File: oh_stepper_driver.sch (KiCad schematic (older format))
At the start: 27 parts, among them P1 CONN_01X04, Q1 CSD18531Q5A, Q2 CSD18531Q5A, Q3 CSD18531Q5A, Q4 CSD18531Q5A, Q5 CSD18531Q5A, Q6 CSD18531Q5A, Q7 CSD18531Q5A, Q8 CSD18531Q5A, U1 DRV8711

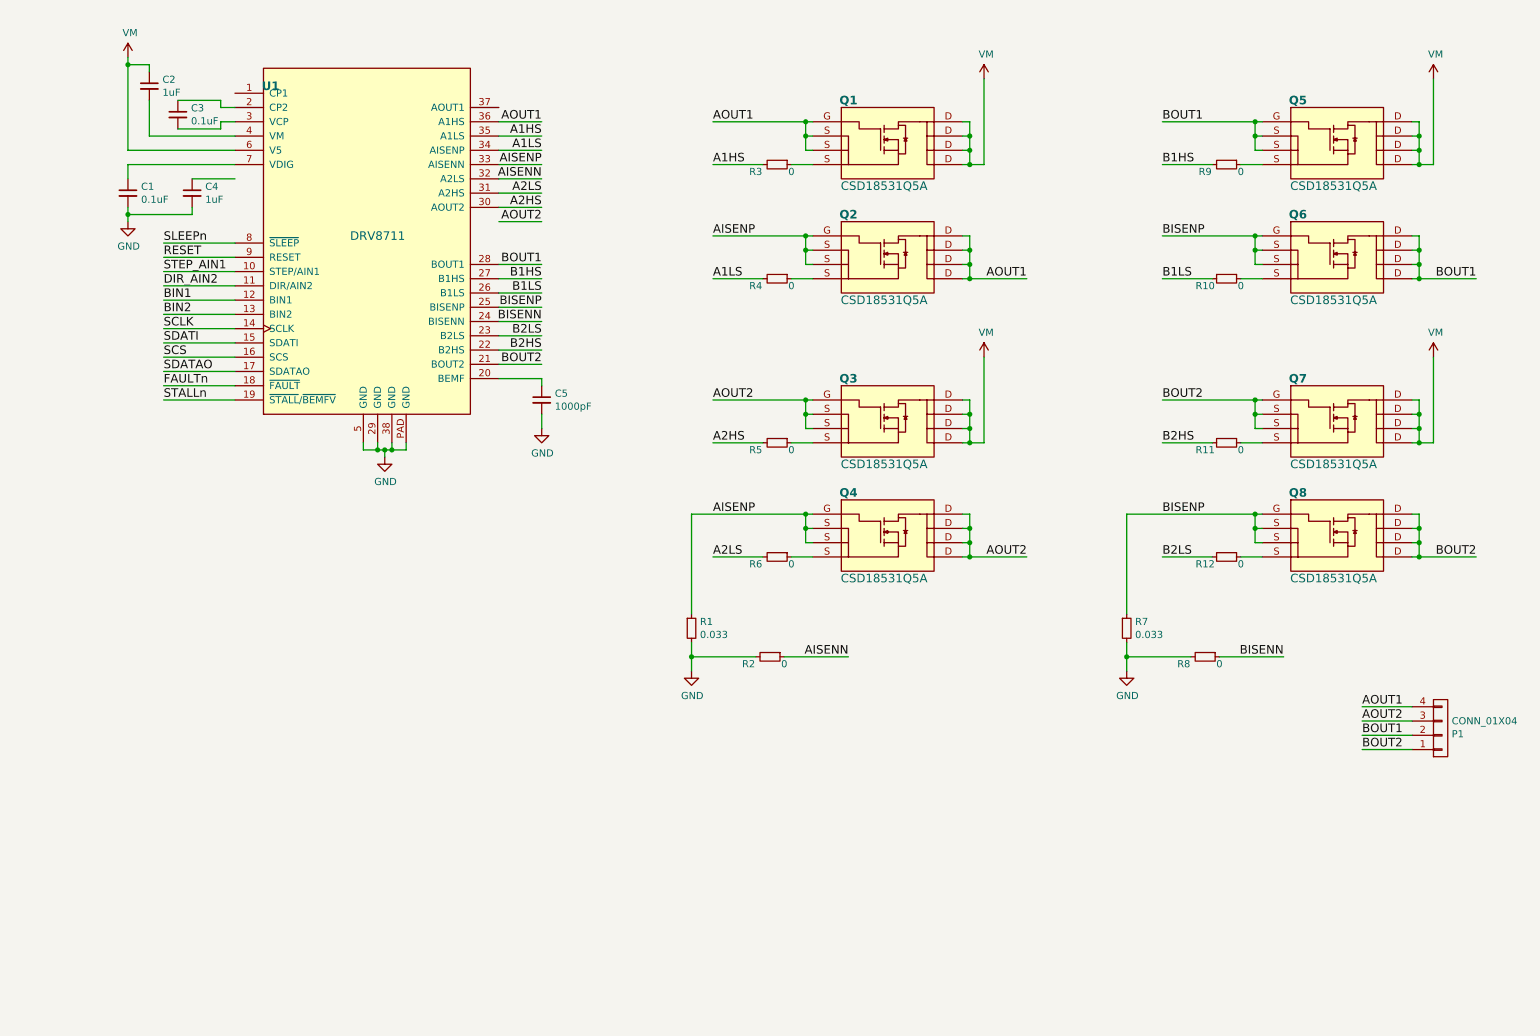
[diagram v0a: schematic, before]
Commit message: FETs sheet added
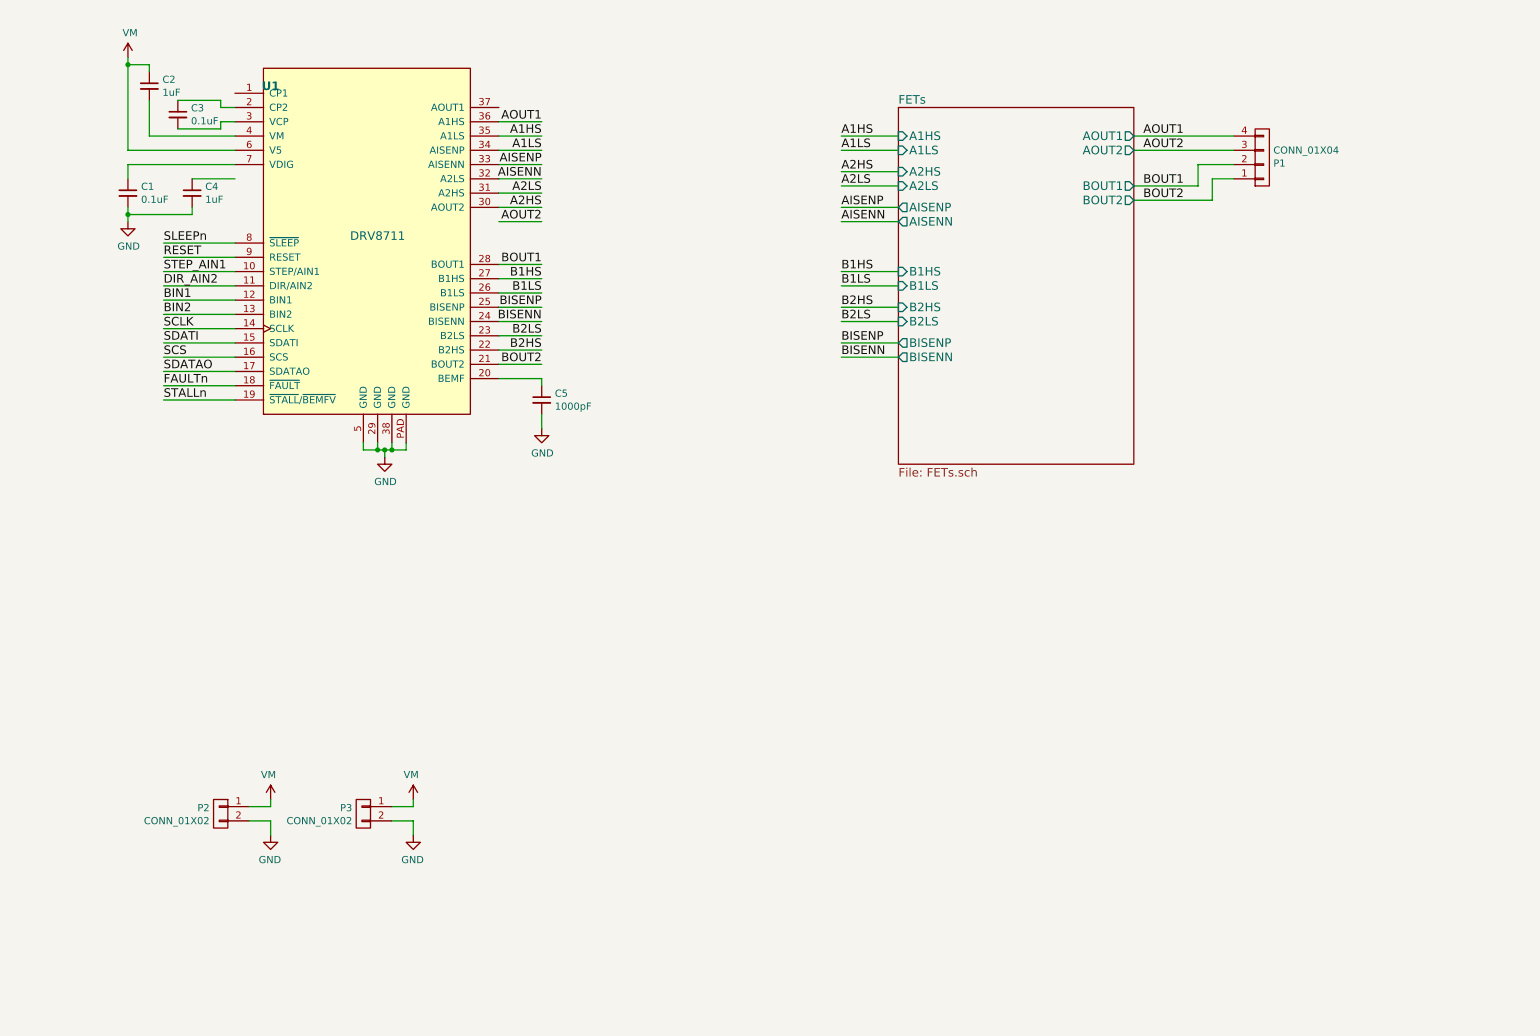
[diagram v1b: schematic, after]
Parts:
- removed Q1, Q2, Q3, Q4, Q5, Q6, Q7, Q8: CSD18531Q5A, oh_stepper:SON5x6_FET, symbol CSD18531Q5A
- removed R1, R7: 0.033, Resistors_SMD:R_2816, symbol R_Small
- removed R10, R11, R12, R3, R4, R5, R6, R9: 0, Resistors_SMD:R_0402, symbol R_Small
- removed R2, R8: 0, Resistors_SMD:R_0603, symbol R_Small
- added P2, P3: CONN_01X02, Connectors:bornier2, symbol CONN_01X02
- C5: footprint (none) -> Capacitors_SMD:C_0402
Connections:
- net GND: now also P2.2 (P2), P3.2 (P2)
- net VM: now also P2.1 (P1), P3.1 (P1)

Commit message: adding decoupling filters
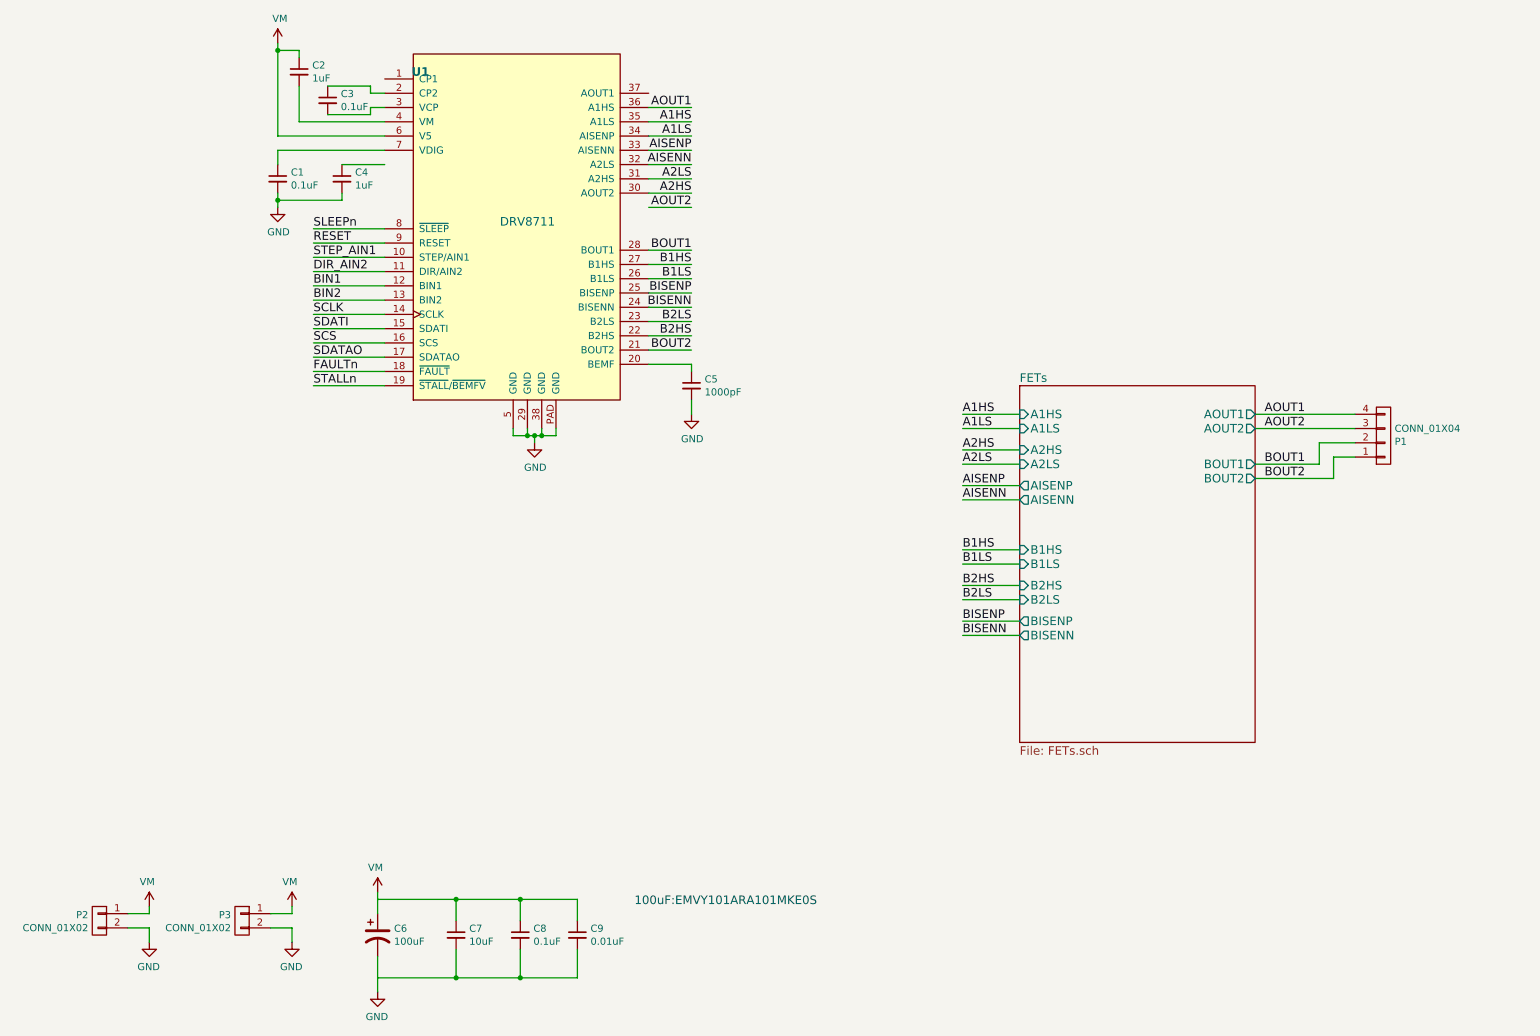
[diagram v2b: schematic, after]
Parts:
- added C6: 100uF, symbol CP1
- added C7: 10uF, symbol C_Small
- added C8: 0.1uF, symbol C_Small
- added C9: 0.01uF, symbol C_Small
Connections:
- wire segments 83 -> 93
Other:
- note added: "100uF:EMVY101ARA101MKE0S"
- moved on the sheet: C1, C2, C3, C4, C5, P1, P2, P3, U1

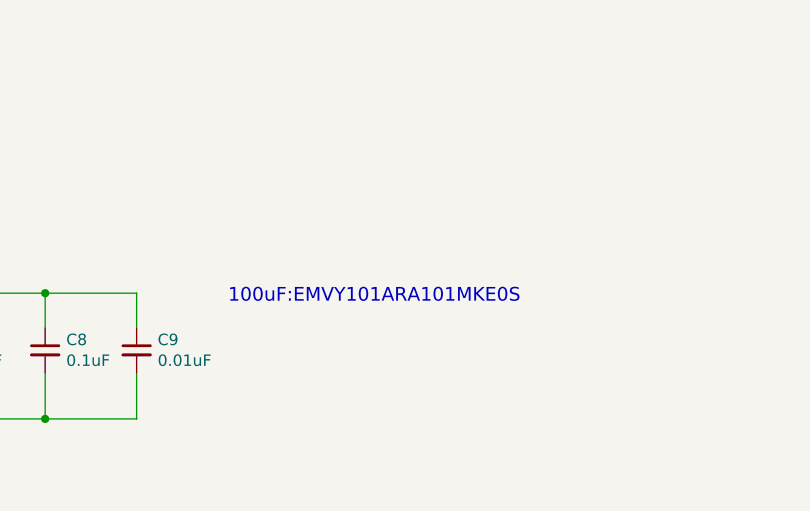
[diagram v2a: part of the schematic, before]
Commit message: adding capacitors to the PCB
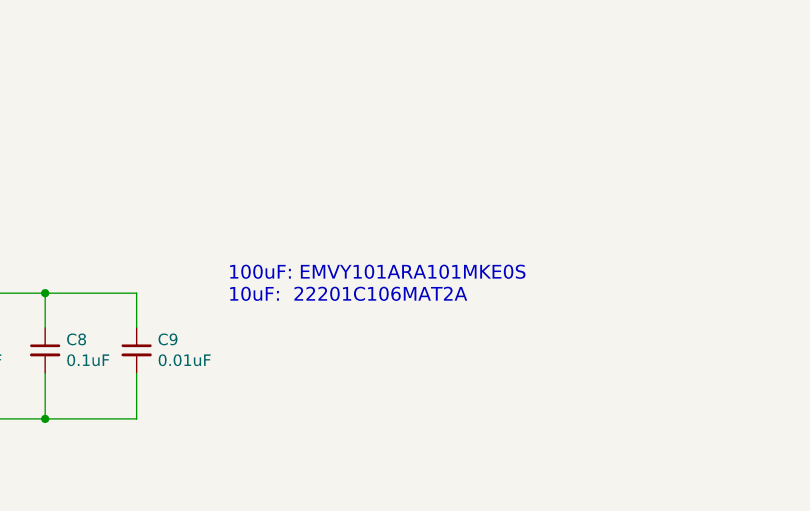
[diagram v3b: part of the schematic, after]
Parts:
- C7: footprint (none) -> Capacitors_SMD:C_2220
- C8, C9: footprint (none) -> Capacitors_SMD:C_0603
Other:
- note added: "100uF: EMVY101ARA101MKE0S \n10uF: 22201C106MAT2A"
- note removed: "100uF:EMVY101ARA101MKE0S"
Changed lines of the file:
@@
 $EndComp
 Text Notes 4800 6950 0    60   ~ 0
- 100uF:EMVY101ARA101MKE0S
+100uF: EMVY101ARA101MKE0S \n10uF:  22201C106MAT2A
 $Comp
 L C_Small C9
@@
 F 0 "C9" H 4492 7196 50  0000 L CNN
 F 1 "0.01uF" H 4492 7105 50  0000 L CNN
-F 2 "" H 4400 7150 50  0000 C CNN
+F 2 "Capacitors_SMD:C_0603" H 4400 7150 50  0001 C CNN
 F 3 "" H 4400 7150 50  0000 C CNN
 	1    4400 7150
@@
 F 0 "C8" H 4092 7196 50  0000 L CNN
 F 1 "0.1uF" H 4092 7105 50  0000 L CNN
-F 2 "" H 4000 7150 50  0000 C CNN
+F 2 "Capacitors_SMD:C_0603" H 4000 7150 50  0001 C CNN
 F 3 "" H 4000 7150 50  0000 C CNN
 	1    4000 7150
@@
 F 0 "C7" H 3642 7196 50  0000 L CNN
 F 1 "10uF" H 3642 7105 50  0000 L CNN
-F 2 "" H 3550 7150 50  0000 C CNN
+F 2 "Capacitors_SMD:C_2220" H 3550 7150 50  0001 C CNN
 F 3 "" H 3550 7150 50  0000 C CNN
 	1    3550 7150

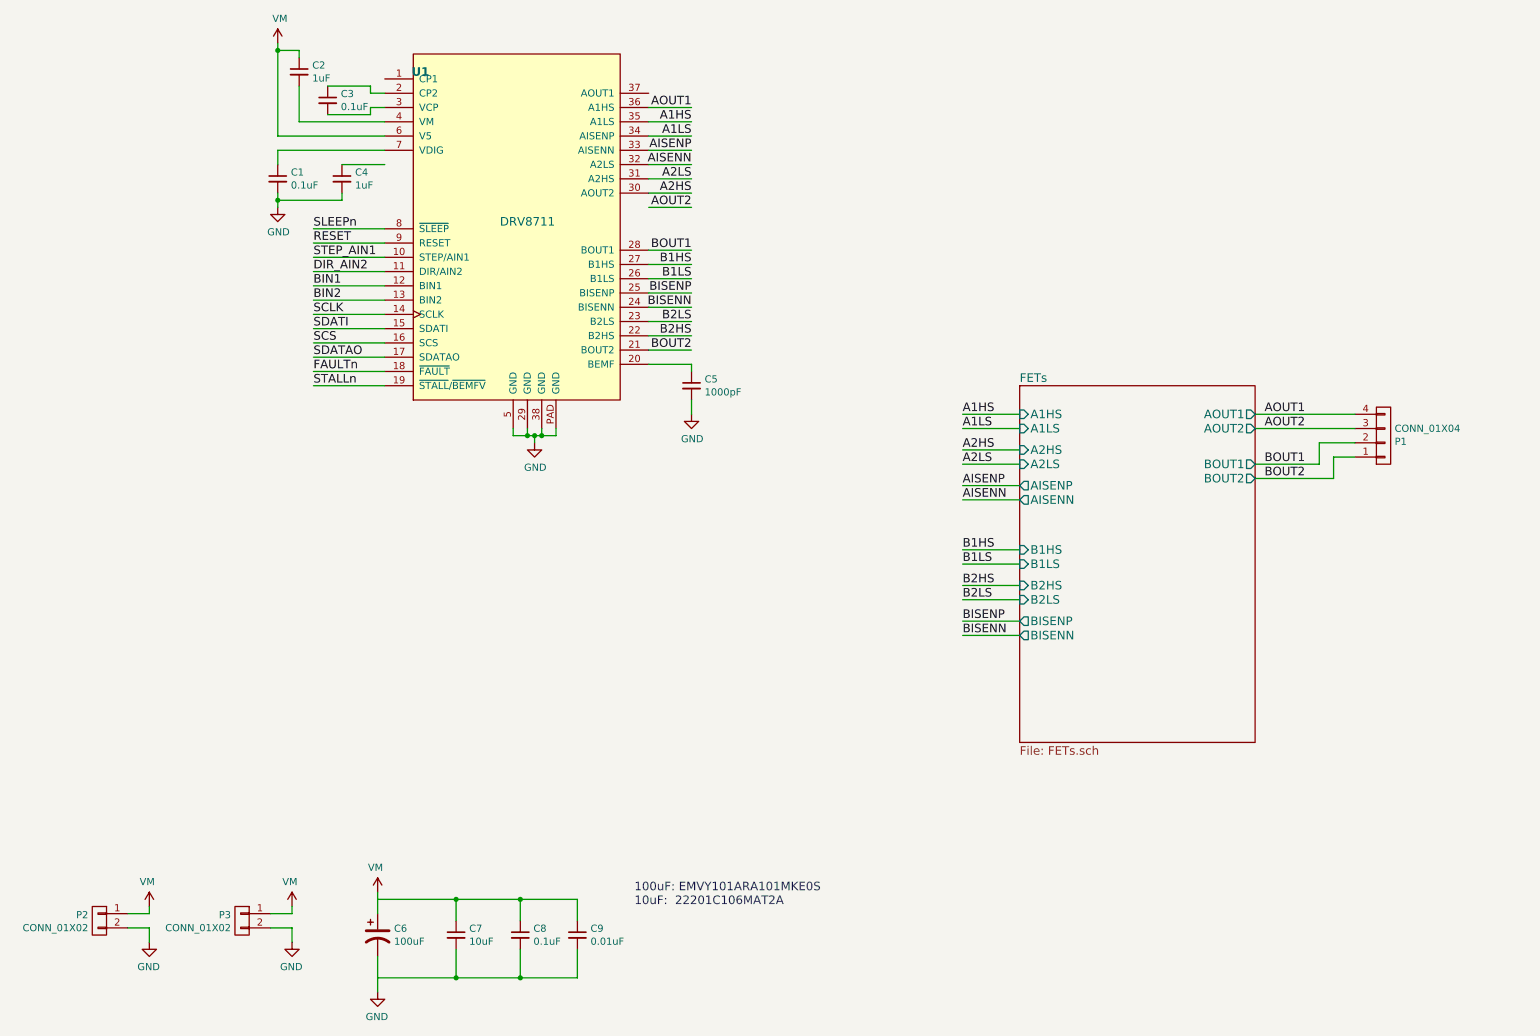
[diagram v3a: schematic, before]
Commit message: stm32f446 added
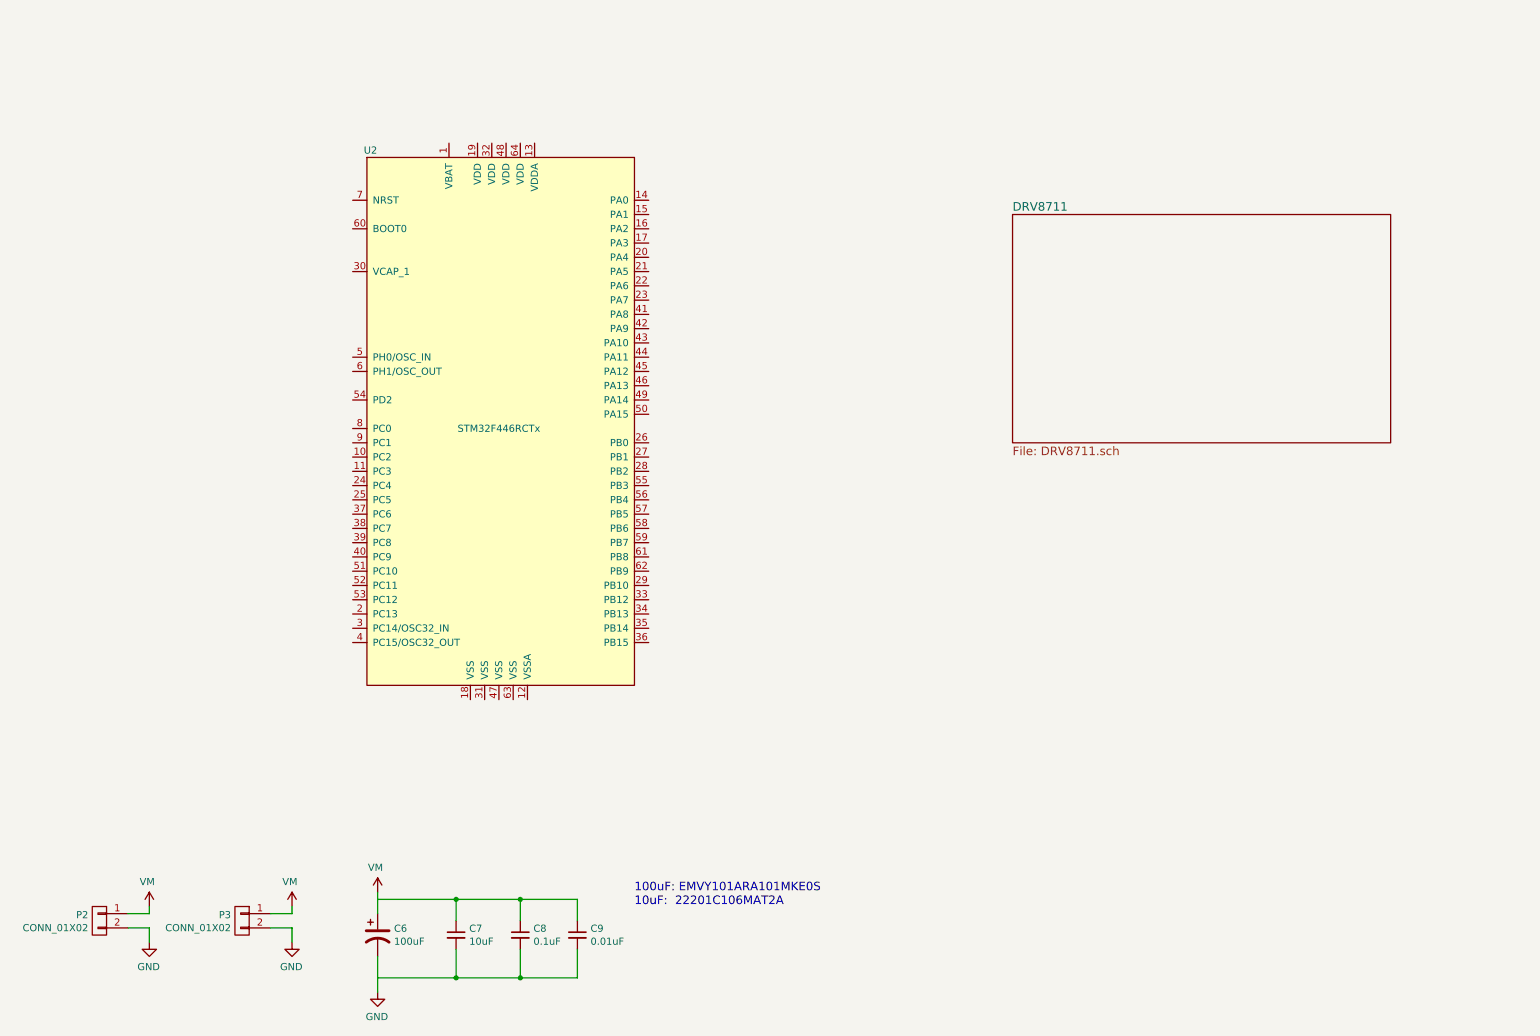
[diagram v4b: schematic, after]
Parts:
- removed C1, C3: 0.1uF, Capacitors_SMD:C_0603, symbol C_Small
- removed C2, C4: 1uF, Capacitors_SMD:C_0603, symbol C_Small
- removed C5: 1000pF, Capacitors_SMD:C_0402, symbol C_Small
- removed P1: CONN_01X04, Connectors:bornier4, symbol CONN_01X04
- removed U1: DRV8711, oh_stepper:HTSSOP_38_Pitch0.5mm, symbol DRV8711
- added U2: STM32F446RCTx, Housings_QFP:LQFP-64_10x10mm_Pitch0.5mm, symbol STM32F446RCTx
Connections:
- net labels removed: A1HS, A1LS, A2HS, A2LS, AISENN, AISENP, AOUT1, AOUT2, B1HS, B1LS, B2HS, B2LS, BIN1, BIN2, BISENN, BISENP, BOUT1, BOUT2, DIR_AIN2, FAULTn, RESET, SCLK, SCS, SDATAO, SDATI, SLEEPn, STALLn, STEP_AIN1
- wire segments 93 -> 18

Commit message: connecting STM32 passives
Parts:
- added C10, C13: 10pF, Capacitors_SMD:C_0402, symbol C_Small
- added C11, C15, C16, C17, C18, C19: 100nF, Capacitors_SMD:C_0402, symbol C_Small
- added C12, C14: 2.2uF, Capacitors_SMD:C_0402, symbol C_Small
- added R13: 47k, Resistors_SMD:R_0402, symbol R
- added X1: ABM8G, SMD:ASDMB, symbol ABM8G
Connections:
- net labels added: +3.3VADC, +3V3, BIN1, BIN2, DIR_AIN2, FAULTn, GNDA, RESET, SCLK, SCS, SDATAO, SDATI, SLEEPn, STALLn, STEP_AIN1
- wire segments 18 -> 73
